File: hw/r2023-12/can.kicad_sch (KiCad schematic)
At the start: 8 parts, among them J7 Conn_02x04_Odd_Even, U7 SN65HVD230

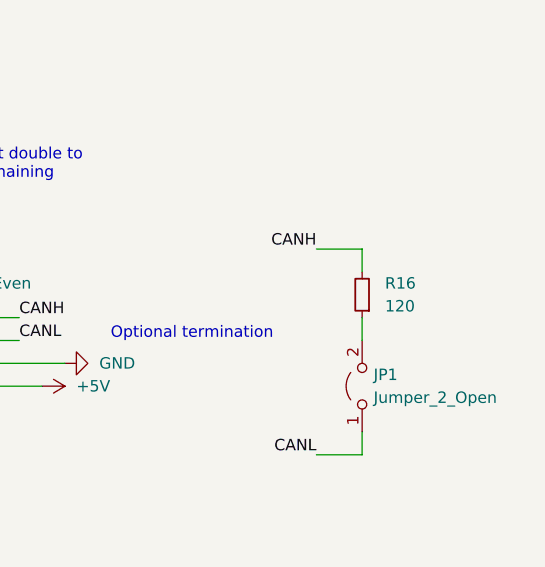
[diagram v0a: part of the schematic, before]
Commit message: r2023_12: add firmware notes and comments on matrix decode
No intentional changes, just text added while working out the firmware.
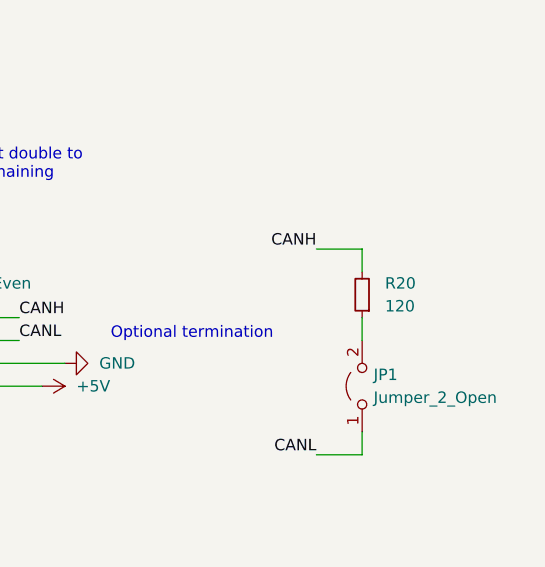
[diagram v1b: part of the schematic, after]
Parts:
- renumbered R16 to R20
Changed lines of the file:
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@@
     (instances
       (project "das-kb4-bara2"
-        (path "/d0e4eaec-96cb-4a0e-a384-5b3e3f5f8d5d/f457a5c4-270e-459d-a4f0-150cf90e3909"
+        (path "/d0e4eaec-96cb-4a0e-a384-5b3e3f5f8d5d/a2d5569b-3e38-48fc-9c53-ff19306ffa54"
           (reference "D4") (unit 1)
         )
-        (path "/d0e4eaec-96cb-4a0e-a384-5b3e3f5f8d5d/7c81bc9d-f306-4c7f-90ce-10f7b22818e4"
-          (reference "D4") (unit 1)
-        )
-        (path "/d0e4eaec-96cb-4a0e-a384-5b3e3f5f8d5d/a2d5569b-3e38-48fc-9c53-ff19306ffa54"
-          (reference "D4") (unit 1)
-        )
       )
     )
@@
     (instances
       (project "das-kb4-bara2"
-        (path "/d0e4eaec-96cb-4a0e-a384-5b3e3f5f8d5d/7c81bc9d-f306-4c7f-90ce-10f7b22818e4"
+        (path "/d0e4eaec-96cb-4a0e-a384-5b3e3f5f8d5d/a2d5569b-3e38-48fc-9c53-ff19306ffa54"
           (reference "#PWR044") (unit 1)
         )
-        (path "/d0e4eaec-96cb-4a0e-a384-5b3e3f5f8d5d/a2d5569b-3e38-48fc-9c53-ff19306ffa54"
-          (reference "#PWR044") (unit 1)
-        )
       )
     )
@@
     (instances
       (project "das-kb4-bara2"
-        (path "/d0e4eaec-96cb-4a0e-a384-5b3e3f5f8d5d/7c81bc9d-f306-4c7f-90ce-10f7b22818e4"
-          (reference "R19") (unit 1)
-        )
         (path "/d0e4eaec-96cb-4a0e-a384-5b3e3f5f8d5d/a2d5569b-3e38-48fc-9c53-ff19306ffa54"
           (reference "R19") (unit 1)
@@
   (symbol (lib_id "power:PWR_FLAG") (at 121.92 83.82 0) (unit 1)
     (in_bom yes) (on_board yes) (dnp no) (fields_autoplaced)
-    (property "Reference" "#FLG01" (at 121.92 81.915 0)
+    (property "Reference" "#FLG04" (at 121.92 81.915 0)
       (effects (font (size 1.27 1.27)) hide)
     )
@@
     (instances
       (project "das-kb4-bara2"
-        (path "/d0e4eaec-96cb-4a0e-a384-5b3e3f5f8d5d/f457a5c4-270e-459d-a4f0-150cf90e3909"
-          (reference "#FLG01") (unit 1)
-        )
         (path "/d0e4eaec-96cb-4a0e-a384-5b3e3f5f8d5d/a2d5569b-3e38-48fc-9c53-ff19306ffa54"
           (reference "#FLG04") (unit 1)
@@
       )
       (project "das-kb4-bara2"
-        (path "/d0e4eaec-96cb-4a0e-a384-5b3e3f5f8d5d/f457a5c4-270e-459d-a4f0-150cf90e3909"
-          (reference "C1") (unit 1)
-        )
-        (path "/d0e4eaec-96cb-4a0e-a384-5b3e3f5f8d5d/7c81bc9d-f306-4c7f-90ce-10f7b22818e4"
+        (path "/d0e4eaec-96cb-4a0e-a384-5b3e3f5f8d5d/a2d5569b-3e38-48fc-9c53-ff19306ffa54"
           (reference "C15") (unit 1)
         )
-        (path "/d0e4eaec-96cb-4a0e-a384-5b3e3f5f8d5d/a2d5569b-3e38-48fc-9c53-ff19306ffa54"
-          (reference "C15") (unit 1)
-        )
       )
     )
@@
     (instances
       (project "das-kb4-bara2"
-        (path "/d0e4eaec-96cb-4a0e-a384-5b3e3f5f8d5d/7c81bc9d-f306-4c7f-90ce-10f7b22818e4"
+        (path "/d0e4eaec-96cb-4a0e-a384-5b3e3f5f8d5d/a2d5569b-3e38-48fc-9c53-ff19306ffa54"
           (reference "#PWR045") (unit 1)
         )
-        (path "/d0e4eaec-96cb-4a0e-a384-5b3e3f5f8d5d/a2d5569b-3e38-48fc-9c53-ff19306ffa54"
-          (reference "#PWR045") (unit 1)
-        )
       )
     )
@@
   (symbol (lib_id "power:GND") (at 175.26 104.14 270) (unit 1)
     (in_bom yes) (on_board yes) (dnp no) (fields_autoplaced)
-    (property "Reference" "#PWR046" (at 168.91 104.14 0)
+    (property "Reference" "#PWR050" (at 168.91 104.14 0)
       (effects (font (size 1.27 1.27)) hide)
     )
@@
     (instances
       (project "das-kb4-bara2"
-        (path "/d0e4eaec-96cb-4a0e-a384-5b3e3f5f8d5d/7c81bc9d-f306-4c7f-90ce-10f7b22818e4"
-          (reference "#PWR046") (unit 1)
-        )
         (path "/d0e4eaec-96cb-4a0e-a384-5b3e3f5f8d5d/a2d5569b-3e38-48fc-9c53-ff19306ffa54"
           (reference "#PWR050") (unit 1)
@@
   (symbol (lib_id "power:GND") (at 40.64 106.68 0) (unit 1)
     (in_bom yes) (on_board yes) (dnp no) (fields_autoplaced)
-    (property "Reference" "#PWR047" (at 40.64 113.03 0)
+    (property "Reference" "#PWR048" (at 40.64 113.03 0)
       (effects (font (size 1.27 1.27)) hide)
     )
@@
     (instances
       (project "das-kb4-bara2"
-        (path "/d0e4eaec-96cb-4a0e-a384-5b3e3f5f8d5d/7c81bc9d-f306-4c7f-90ce-10f7b22818e4"
-          (reference "#PWR047") (unit 1)
-        )
         (path "/d0e4eaec-96cb-4a0e-a384-5b3e3f5f8d5d/a2d5569b-3e38-48fc-9c53-ff19306ffa54"
           (reference "#PWR048") (unit 1)
@@
     (instances
       (project "das-kb4-bara2"
-        (path "/d0e4eaec-96cb-4a0e-a384-5b3e3f5f8d5d/7c81bc9d-f306-4c7f-90ce-10f7b22818e4"
+        (path "/d0e4eaec-96cb-4a0e-a384-5b3e3f5f8d5d/a2d5569b-3e38-48fc-9c53-ff19306ffa54"
           (reference "U7") (unit 1)
         )
-        (path "/d0e4eaec-96cb-4a0e-a384-5b3e3f5f8d5d/a2d5569b-3e38-48fc-9c53-ff19306ffa54"
-          (reference "U7") (unit 1)
-        )
       )
     )
@@
   (symbol (lib_id "power:GND") (at 152.4 119.38 0) (unit 1)
     (in_bom yes) (on_board yes) (dnp no) (fields_autoplaced)
-    (property "Reference" "#PWR045" (at 152.4 125.73 0)
+    (property "Reference" "#PWR049" (at 152.4 125.73 0)
       (effects (font (size 1.27 1.27)) hide)
     )
@@
     (instances
       (project "das-kb4-bara2"
-        (path "/d0e4eaec-96cb-4a0e-a384-5b3e3f5f8d5d/7c81bc9d-f306-4c7f-90ce-10f7b22818e4"
-          (reference "#PWR045") (unit 1)
-        )
         (path "/d0e4eaec-96cb-4a0e-a384-5b3e3f5f8d5d/a2d5569b-3e38-48fc-9c53-ff19306ffa54"
           (reference "#PWR049") (unit 1)
@@
   (symbol (lib_id "power:GND") (at 198.12 104.14 90) (unit 1)
     (in_bom yes) (on_board yes) (dnp no) (fields_autoplaced)
-    (property "Reference" "#PWR046" (at 204.47 104.14 0)
+    (property "Reference" "#PWR047" (at 204.47 104.14 0)
       (effects (font (size 1.27 1.27)) hide)
     )
@@
     (instances
       (project "das-kb4-bara2"
-        (path "/d0e4eaec-96cb-4a0e-a384-5b3e3f5f8d5d/7c81bc9d-f306-4c7f-90ce-10f7b22818e4"
-          (reference "#PWR046") (unit 1)
-        )
         (path "/d0e4eaec-96cb-4a0e-a384-5b3e3f5f8d5d/a2d5569b-3e38-48fc-9c53-ff19306ffa54"
           (reference "#PWR047") (unit 1)
@@
   (symbol (lib_id "Device:R_Small") (at 231.14 96.52 180) (unit 1)
     (in_bom yes) (on_board yes) (dnp no) (fields_autoplaced)
-    (property "Reference" "R16" (at 233.68 95.25 0)
+    (property "Reference" "R20" (at 233.68 95.25 0)
       (effects (font (size 1.27 1.27)) (justify right))
     )
@@
     (instances
       (project "das-kb4-bara2"
-        (path "/d0e4eaec-96cb-4a0e-a384-5b3e3f5f8d5d/7c81bc9d-f306-4c7f-90ce-10f7b22818e4"
-          (reference "R16") (unit 1)
-        )
         (path "/d0e4eaec-96cb-4a0e-a384-5b3e3f5f8d5d/a2d5569b-3e38-48fc-9c53-ff19306ffa54"
           (reference "R20") (unit 1)
